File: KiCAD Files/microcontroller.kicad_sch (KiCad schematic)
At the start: 49 parts, among them IC5 AZ1117IH-3.3TRG1, J3 TSW-103-14-S-D, J4 TSW-103-14-S-D, J7 TSW-105-05-F-S, U1 STM32H7A3RGTx, Y1 ABM8G-48.000MHZ-18-D2Y-T

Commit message: finalized 99% of pcb
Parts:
- removed TP13, TP15, TP16: TestPoint, TestPoint:TestPoint_THTPad_D1.5mm_Drill0.7mm, symbol Connector:TestPoint
- TP1, TP10, TP11, TP12, TP14, TP2, TP3, TP4, TP5, TP6, TP7, TP8, TP9: footprint TestPoint:TestPoint_THTPad_D1.5mm_Drill0.7mm -> TestPoint:TestPoint_THTPad_D1.0mm_Drill0.5mm
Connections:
- net PA0/CS1 is gone; now on net PC9/CS1: TP12.1
- net PA1/CS2 is gone; now on net PB1/CS2: TP11.1
- net PA2/CS3 is gone; now on net PC3/CS3: TP10.1
- net PA3/CS4 is gone; now on net PH1/CS4: TP9.1
- net PB8/KeyC3 is gone; now on net PB5/KeyC3: TP14.1
- net PC10/HOLD4 is gone; now on net PB6/HOLD4: TP8.1
- net PC2/WP1 is gone; now on net PC7/WP1: TP1.1
- net PC3/WP2 is gone; now on net PB0/WP2: TP2.1
- net PC4/WP3 is gone; now on net PC2/WP3: TP3.1
- net PC5/WP4 is gone; now on net PC0/WP4: TP4.1
- net PC7/HOLD2 is gone; now on net PA2/HOLD2: TP6.1
- net PC9/HOLD3 is gone; now on net PC1/HOLD3: TP7.1
- net PC3/CS3: now reaches U1.11 (PC3)
- no-connect marks 15 -> 14

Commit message: updated files with 3d models
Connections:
- net BOOT0: now reaches R2.1, U1.60 (BOOT0)
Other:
- moved on the sheet: TP10, TP11, TP12, TP5, TP6, TP7, TP8, TP9
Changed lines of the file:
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@@
 		)
 	)
+	(label "BOOT0"
+		(at 34.29 36.83 0)
+		(effects
+			(font
+				(size 1.27 1.27)
+			)
+			(justify left bottom)
+		)
+	)
 	(global_label "PC6{slash}HOLD1"
 		(shape input)
@@
 	(global_label "PC6{slash}HOLD1"
 		(shape input)
-		(at 129.54 139.7 180)
+		(at 128.27 144.78 180)
 		(fields_autoplaced yes)
 		(effects
@@
 		)
 		(property "Intersheetrefs" "${INTERSHEET_REFS}"
-			(at 115.3062 139.7 0)
+			(at 114.0362 144.78 0)
 			(effects
 				(font
@@
 	(global_label "PB1{slash}CS2"
 		(shape input)
-		(at 129.54 158.75 180)
+		(at 127 167.64 180)
 		(fields_autoplaced yes)
 		(effects
@@
 		)
 		(property "Intersheetrefs" "${INTERSHEET_REFS}"
-			(at 117.7858 158.75 0)
+			(at 115.2458 167.64 0)
 			(effects
 				(font
@@
 	(global_label "PH1{slash}CS4"
 		(shape input)
-		(at 129.54 151.13 180)
+		(at 127 160.02 180)
 		(fields_autoplaced yes)
 		(effects
@@
 		)
 		(property "Intersheetrefs" "${INTERSHEET_REFS}"
-			(at 117.7253 151.13 0)
+			(at 115.1853 160.02 0)
 			(effects
 				(font
@@
 	(global_label "PC1{slash}HOLD3"
 		(shape input)
-		(at 129.54 144.78 180)
+		(at 128.27 149.86 180)
 		(fields_autoplaced yes)
 		(effects
@@
 		)
 		(property "Intersheetrefs" "${INTERSHEET_REFS}"
-			(at 115.3062 144.78 0)
+			(at 114.0362 149.86 0)
 			(effects
 				(font
@@
 	(global_label "PB6{slash}HOLD4"
 		(shape input)
-		(at 129.54 147.32 180)
+		(at 128.27 152.4 180)
 		(fields_autoplaced yes)
 		(effects
@@
 		)
 		(property "Intersheetrefs" "${INTERSHEET_REFS}"
-			(at 115.3062 147.32 0)
+			(at 114.0362 152.4 0)
 			(effects
 				(font
@@
 	(global_label "PA2{slash}HOLD2"
 		(shape input)
-		(at 129.54 142.24 180)
+		(at 128.27 147.32 180)
 		(fields_autoplaced yes)
 		(effects
@@
 		)
 		(property "Intersheetrefs" "${INTERSHEET_REFS}"
-			(at 115.4876 142.24 0)
+			(at 114.2176 147.32 0)
 			(effects
 				(font
@@
 	(global_label "PC9{slash}CS1"
 		(shape input)
-		(at 129.54 162.56 180)
+		(at 127 171.45 180)
 		(fields_autoplaced yes)
 		(effects
@@
 		)
 		(property "Intersheetrefs" "${INTERSHEET_REFS}"
-			(at 117.7858 162.56 0)
+			(at 115.2458 171.45 0)
 			(effects
 				(font
@@
 	(global_label "PC3{slash}CS3"
 		(shape input)
-		(at 129.54 154.94 180)
+		(at 127 163.83 180)
 		(fields_autoplaced yes)
 		(effects
@@
 		)
 		(property "Intersheetrefs" "${INTERSHEET_REFS}"
-			(at 117.7858 154.94 0)
+			(at 115.2458 163.83 0)
 			(effects
 				(font
@@
 	(symbol
 		(lib_id "Connector:TestPoint")
-		(at 129.54 147.32 270)
+		(at 128.27 152.4 270)
 		(unit 1)
 		(exclude_from_sim no)
@@
 		(dnp no)
 		(property "Reference" "TP8"
-			(at 136.398 147.828 90)
+			(at 135.128 152.908 90)
 			(effects
 				(font
@@
 		)
 		(property "Value" "TestPoint"
-			(at 141.732 147.574 90)
+			(at 140.462 152.654 90)
 			(effects
 				(font
@@
 		)
 		(property "Footprint" "TestPoint:TestPoint_THTPad_D1.0mm_Drill0.5mm"
-			(at 129.54 152.4 0)
+			(at 128.27 157.48 0)
 			(effects
 				(font
@@
 		)
 		(property "Datasheet" "~"
-			(at 129.54 152.4 0)
+			(at 128.27 157.48 0)
 			(effects
 				(font
@@
 		)
 		(property "Description" "test point"
-			(at 129.54 147.32 0)
+			(at 128.27 152.4 0)
 			(effects
 				(font
@@
 	(symbol
 		(lib_id "Connector:TestPoint")
-		(at 129.54 142.24 270)
+		(at 128.27 147.32 270)
 		(unit 1)
 		(exclude_from_sim no)
@@
 		(dnp no)
 		(property "Reference" "TP6"
-			(at 135.128 142.494 90)
+			(at 133.858 147.574 90)
 			(effects
 				(font
@@
 		)
 		(property "Value" "TestPoint"
-			(at 141.224 141.478 90)
+			(at 139.954 146.558 90)
 			(effects
 				(font
@@
 		)
 		(property "Footprint" "TestPoint:TestPoint_THTPad_D1.0mm_Drill0.5mm"
-			(at 129.54 147.32 0)
+			(at 128.27 152.4 0)
 			(effects
 				(font
@@
 		)
 		(property "Datasheet" "~"
-			(at 129.54 147.32 0)
+			(at 128.27 152.4 0)
 			(effects
 				(font
@@
 		)
 		(property "Description" "test point"
-			(at 129.54 142.24 0)
+			(at 128.27 147.32 0)
 			(effects
 				(font
@@
 	(symbol
 		(lib_id "Connector:TestPoint")
-		(at 129.54 154.94 270)
+		(at 127 163.83 270)
 		(unit 1)
 		(exclude_from_sim no)
@@
 		(dnp no)
 		(property "Reference" "TP10"
-			(at 135.128 155.194 90)
+			(at 132.588 164.084 90)
 			(effects
 				(font
@@
 		)
 		(property "Value" "TestPoint"
-			(at 141.224 154.178 90)
+			(at 138.684 163.068 90)
 			(effects
 				(font
@@
 		)
 		(property "Footprint" "TestPoint:TestPoint_THTPad_D1.0mm_Drill0.5mm"
-			(at 129.54 160.02 0)
+			(at 127 168.91 0)
 			(effects
 				(font
@@
 		)
 		(property "Datasheet" "~"
-			(at 129.54 160.02 0)
+			(at 127 168.91 0)
 			(effects
 				(font
@@
 		)
 		(property "Description" "test point"
-			(at 129.54 154.94 0)
+			(at 127 163.83 0)
 			(effects
 				(font
@@
 	(symbol
 		(lib_id "Connector:TestPoint")
-		(at 129.54 162.56 270)
+		(at 127 171.45 270)
 		(unit 1)
 		(exclude_from_sim no)
@@
 		(dnp no)
 		(property "Reference" "TP12"
-			(at 136.398 163.068 90)
+			(at 133.858 171.958 90)
 			(effects
 				(font
@@
 		)
 		(property "Value" "TestPoint"
-			(at 141.732 162.814 90)
+			(at 139.192 171.704 90)
 			(effects
 				(font
@@
 		)
 		(property "Footprint" "TestPoint:TestPoint_THTPad_D1.0mm_Drill0.5mm"
-			(at 129.54 167.64 0)
+			(at 127 176.53 0)
 			(effects
 				(font
@@
 		)
 		(property "Datasheet" "~"
-			(at 129.54 167.64 0)
+			(at 127 176.53 0)
 			(effects
 				(font
@@
 		)
 		(property "Description" "test point"
-			(at 129.54 162.56 0)
+			(at 127 171.45 0)
 			(effects
 				(font
@@
 	(symbol
 		(lib_id "Connector:TestPoint")
-		(at 129.54 139.7 270)
+		(at 128.27 144.78 270)
 		(unit 1)
 		(exclude_from_sim no)
@@
 		(dnp no)
 		(property "Reference" "TP5"
-			(at 136.652 139.446 90)
+			(at 135.382 144.526 90)
 			(effects
 				(font
@@
 		)
 		(property "Value" "TestPoint"
-			(at 144.018 139.192 90)
+			(at 142.748 144.272 90)
 			(effects
 				(font
@@
 		)
 		(property "Footprint" "TestPoint:TestPoint_THTPad_D1.0mm_Drill0.5mm"
-			(at 129.54 144.78 0)
+			(at 128.27 149.86 0)
 			(effects
 				(font
@@
 		)
 		(property "Datasheet" "~"
-			(at 129.54 144.78 0)
+			(at 128.27 149.86 0)
 			(effects
 				(font
@@
 		)
 		(property "Description" "test point"
-			(at 129.54 139.7 0)
+			(at 128.27 144.78 0)
 			(effects
 				(font
@@
 	(symbol
 		(lib_id "Connector:TestPoint")
-		(at 129.54 151.13 270)
+		(at 127 160.02 270)
 		(unit 1)
 		(exclude_from_sim no)
@@
 		(dnp no)
 		(property "Reference" "TP9"
-			(at 136.652 150.876 90)
+			(at 134.112 159.766 90)
 			(effects
 				(font
@@
 		)
 		(property "Value" "TestPoint"
-			(at 144.018 150.622 90)
+			(at 141.478 159.512 90)
 			(effects
 				(font
@@
 		)
 		(property "Footprint" "TestPoint:TestPoint_THTPad_D1.0mm_Drill0.5mm"
-			(at 129.54 156.21 0)
+			(at 127 165.1 0)
 			(effects
 				(font
@@
 		)
 		(property "Datasheet" "~"
-			(at 129.54 156.21 0)
+			(at 127 165.1 0)
 			(effects
 				(font
@@
 		)
 		(property "Description" "test point"
-			(at 129.54 151.13 0)
+			(at 127 160.02 0)
 			(effects
 				(font
@@
 		(on_board yes)
 		(dnp no)
-		(fields_autoplaced yes)
 		(property "Reference" "U1"
-			(at 63.1541 118.11 0)
+			(at 75.692 119.126 0)
 			(effects
 				(font
@@
 		)
 		(property "Value" "STM32H7A3RGTx"
-			(at 63.1541 120.65 0)
+			(at 75.692 121.666 0)
 			(effects
 				(font
@@
 	(symbol
 		(lib_id "Connector:TestPoint")
-		(at 129.54 158.75 270)
+		(at 127 167.64 270)
 		(unit 1)
 		(exclude_from_sim no)
@@
 		(dnp no)
 		(property "Reference" "TP11"
-			(at 136.398 159.258 90)
+			(at 133.858 168.148 90)
 			(effects
 				(font
@@
 		)
 		(property "Value" "TestPoint"
-			(at 141.732 159.004 90)
+			(at 139.192 167.894 90)
 			(effects
 				(font
@@
 		)
 		(property "Footprint" "TestPoint:TestPoint_THTPad_D1.0mm_Drill0.5mm"
-			(at 129.54 163.83 0)
+			(at 127 172.72 0)
 			(effects
 				(font
@@
 		)
 		(property "Datasheet" "~"
-			(at 129.54 163.83 0)
+			(at 127 172.72 0)
 			(effects
 				(font
@@
 		)
 		(property "Description" "test point"
-			(at 129.54 158.75 0)
+			(at 127 167.64 0)
 			(effects
 				(font
@@
 	(symbol
 		(lib_id "Connector:TestPoint")
-		(at 129.54 144.78 270)
+		(at 128.27 149.86 270)
 		(unit 1)
 		(exclude_from_sim no)
@@
 		(dnp no)
 		(property "Reference" "TP7"
-			(at 136.398 145.288 90)
+			(at 135.128 150.368 90)
 			(effects
 				(font
@@
 		)
 		(property "Value" "TestPoint"
-			(at 141.732 145.034 90)
+			(at 140.462 150.114 90)
 			(effects
 				(font
@@
 		)
 		(property "Footprint" "TestPoint:TestPoint_THTPad_D1.0mm_Drill0.5mm"
-			(at 129.54 149.86 0)
+			(at 128.27 154.94 0)
 			(effects
 				(font
@@
 		)
 		(property "Datasheet" "~"
-			(at 129.54 149.86 0)
+			(at 128.27 154.94 0)
 			(effects
 				(font
@@
 		)
 		(property "Description" "test point"
-			(at 129.54 144.78 0)
+			(at 128.27 149.86 0)
 			(effects
 				(font

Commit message: made most of the easy changes for the pcb
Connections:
- net D+ is gone; now on net GND: J3.3
- net D- is gone; now on net GND: J3.5
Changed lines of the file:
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@@
+	)
+	(junction
+		(at 130.81 26.67)
+		(diameter 0)
+		(color 0 0 0 0)
 	)
 	(junction
@@
 	)
 	(junction
+		(at 130.81 29.21)
+		(diameter 0)
+		(color 0 0 0 0)
+	)
+	(junction
 		(at 45.72 162.56)
 		(diameter 0)
@@
 	(wire
 		(pts
+			(xy 130.81 26.67) (xy 130.81 29.21)
+		)
+		(stroke
+			(width 0)
+			(type default)
+		)
+	)
+	(wire
+		(pts
 			(xy 223.52 83.82) (xy 215.9 83.82)
 		)
@@
 		(pts
 			(xy 76.2 31.75) (xy 77.47 31.75)
+		)
+		(stroke
+			(width 0)
+			(type default)
+		)
+	)
+	(wire
+		(pts
+			(xy 130.81 29.21) (xy 130.81 31.75)
 		)
 		(stroke
@@
 		)
 	)
-	(global_label "D+"
-		(shape input)
-		(at 130.81 29.21 180)
-		(fields_autoplaced yes)
-		(effects
-			(font
-				(size 1.27 1.27)
-				(color 0 0 0 1)
-			)
-			(justify right)
-		)
-		(property "Intersheetrefs" "${INTERSHEET_REFS}"
-			(at 124.9824 29.21 0)
-			(effects
-				(font
-					(size 1.27 1.27)
-				)
-				(justify right)
-				(hide yes)
-			)
-		)
-	)
 	(global_label "PC1{slash}HOLD3"
 		(shape input)
@@
 			(effects
 				(font
-					(size 1.27 1.27)
-				)
-				(justify right)
-				(hide yes)
-			)
-		)
-	)
-	(global_label "D-"
-		(shape input)
-		(at 130.81 31.75 180)
-		(fields_autoplaced yes)
-		(effects
-			(font
-				(size 1.27 1.27)
-				(color 0 0 0 1)
-			)
-			(justify right)
-		)
-		(property "Intersheetrefs" "${INTERSHEET_REFS}"
-			(at 124.9824 31.75 0)
-			(effects
-				(font

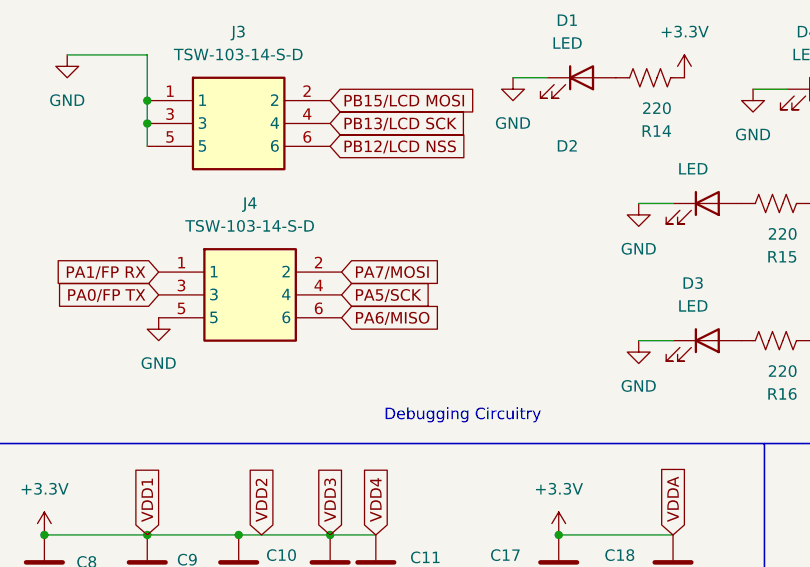
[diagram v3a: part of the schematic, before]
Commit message: finalized pcb design (miso line is still cooked but better)
finished up most of the pcb design work, need to check if we can route spi signals under the flash ic (or is it smth we look up in datasheet)?
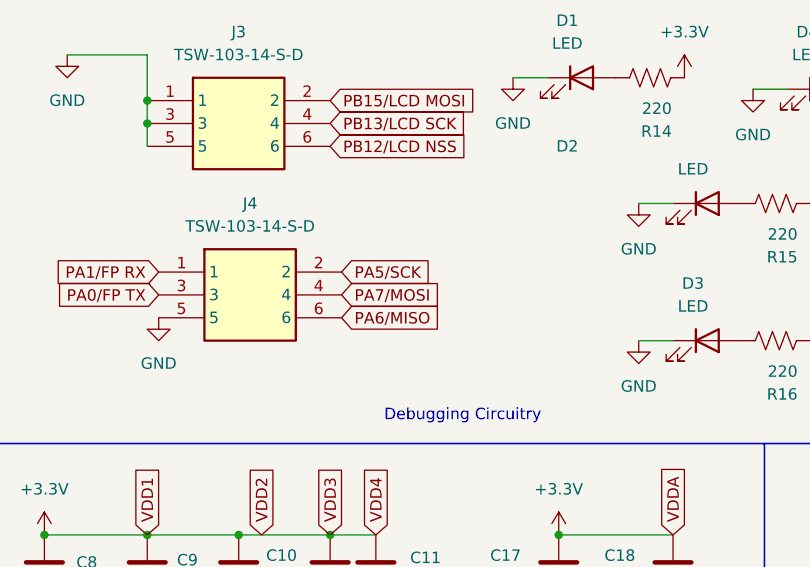
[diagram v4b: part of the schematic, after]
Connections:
- net PA5/SCK: now also J4.2; no longer J4.4
- net PA7/MOSI: now also J4.4; no longer J4.2

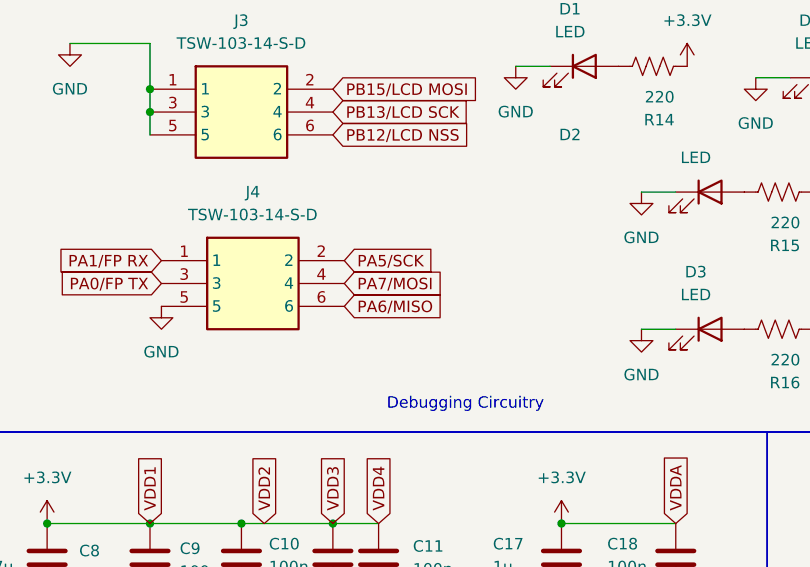
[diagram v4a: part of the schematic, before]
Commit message: made VBAT pad bigger
hi Joshua
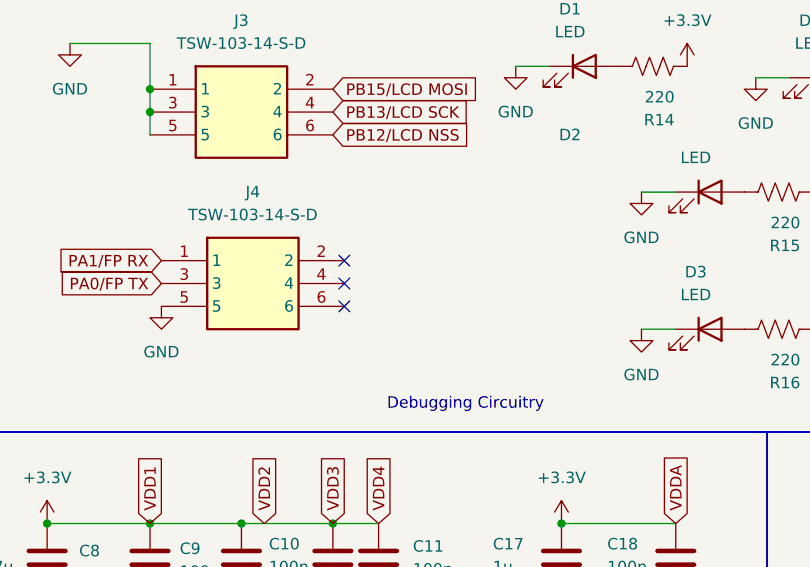
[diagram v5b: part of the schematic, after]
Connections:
- net PA5/SCK: no longer J4.2
- net PA6/MISO: no longer J4.6
- net PA7/MOSI: no longer J4.4
- no-connect marks 14 -> 17
